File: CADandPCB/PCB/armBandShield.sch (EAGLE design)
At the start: 32 parts, among them Q1 BSS138, Q2 BSS138, U2 MPU-6050-1

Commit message: Initial layout 95% complete
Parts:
- removed FSR_HEADERS: (no value), SparkFun-Connectors:CONN_08"
- added J1: FSR_HEADERS_1, SparkFun-Connectors:CONN_04
- added J2: FSR_HEADERS_2, SparkFun-Connectors:CONN_04
- BT_HEADERS: value (none) -> J5
- LEFT_HEADER: value (none) -> J3
- RIGHT_HEADER: value (none) -> J4; device SparkFun-Connectors:CONN_15 -> SparkFun-Connectors:CONN_14
- SWITCH_HEADERS: value 455-1750-1-ND -> J8
- VCC_HEADERS: value (none) -> J6; device SparkFun-Connectors:CONN_02 -> SparkFun-Connectors:CONN_02PTH3
- VIN_HEADERS: value (none) -> J7
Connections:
- net A0: now also RIGHT_HEADER.3; no longer RIGHT_HEADER.4
- net A4/SDA/HIGH: now also RIGHT_HEADER.7; no longer RIGHT_HEADER.8
- net A5/SCL/HIGH: now also RIGHT_HEADER.8; no longer RIGHT_HEADER.9
- net FSR1: now also J2.1; no longer FSR_HEADERS.1
- net FSR2: now also J2.2; no longer FSR_HEADERS.2
- net FSR3: now also J2.3; no longer FSR_HEADERS.3
- net FSR4: now also J2.4; no longer FSR_HEADERS.4
- net FSR5: now also J1.1; no longer FSR_HEADERS.5
- net FSR6: now also J1.2; no longer FSR_HEADERS.6
- net FSR7: now also J1.3; no longer FSR_HEADERS.7
- net FSR8: now also J1.4; no longer FSR_HEADERS.8
- net GND: now also RIGHT_HEADER.13; no longer RIGHT_HEADER.14
- net VCC: now also RIGHT_HEADER.11; no longer RIGHT_HEADER.12
- net VCC_2: now also RIGHT_HEADER.1; no longer RIGHT_HEADER.2
- net VIN: now also RIGHT_HEADER.14; no longer RIGHT_HEADER.15

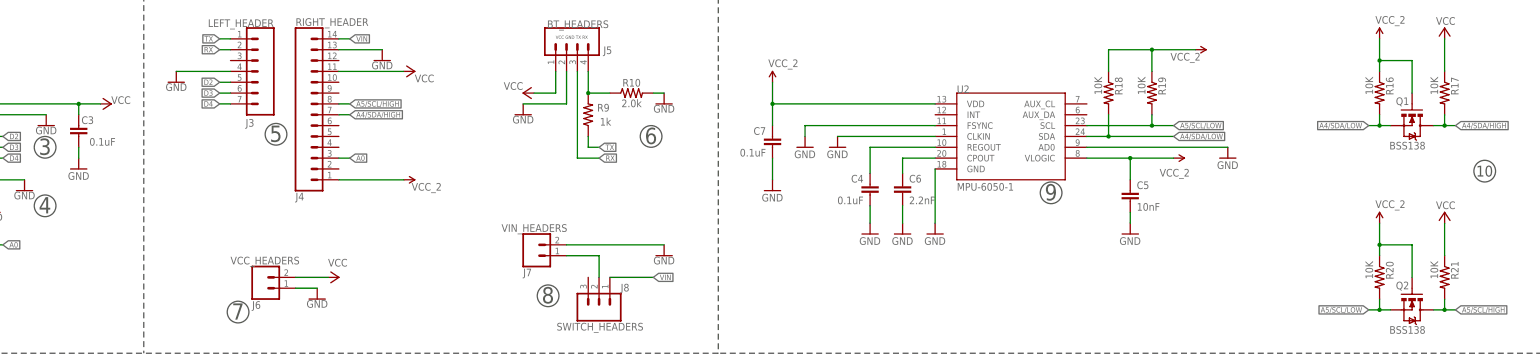
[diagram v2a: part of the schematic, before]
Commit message: Update trace sizes, pad extensions, silkscreen, and some routing.
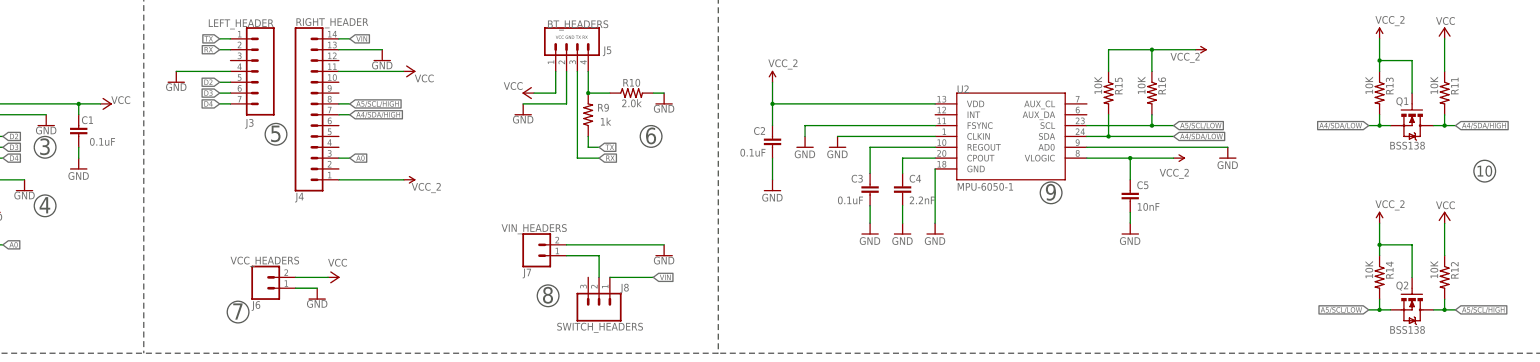
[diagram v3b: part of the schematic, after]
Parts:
- removed C6: 2.2nF, SparkFun-Capacitors:2.2NF/2200PF-0603-50V-10%
- removed R19: 10K, SparkFun-Resistors:10KOHM-1/10W-1%(0603)0603
- added C1: 0.1uF, SparkFun-Capacitors:0.1UF-25V(+80/-20%)(0603)
- added R13: 10K, SparkFun:RESISTOR0603-RES
- C4: value 0.1uF -> 2.2nF; device SparkFun-Capacitors:0.1UF-25V(+80/-20%)(0603) -> SparkFun-Capacitors:2.2NF/2200PF-0603-50V-10%
- R16: device SparkFun:RESISTOR0603-RES -> SparkFun-Resistors:10KOHM-1/10W-1%(0603)0603
- renumbered C7 to C2, R17 to R11, R18 to R15, R20 to R14, R21 to R12
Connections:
- net A4/SDA/LOW: now also R13.2; no longer R16.2
- net A5/SCL/LOW: now also R16.2; no longer R19.2
- net GND: now also C1.2; no longer C6.2
- net N$3: now also C4.1; no longer C6.1
- net N$5: now also C3.1; no longer C4.1
- net VCC: now also C1.1; no longer C3.1
- net VCC_2: now also R13.1; no longer R19.1
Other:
- moved on the sheet: C3, C4, R16

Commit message: Commit Gerber files and final rev 1 of board.
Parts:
- removed SWITCH_HEADERS: J8, SparkFun-Connectors:CONN_03
- added J10, J8, J9: (no value), SparkFun-Connectors:CONN_01
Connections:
- net N$1: now also J9.1; no longer SWITCH_HEADERS.2
- net VIN: now also J10.1; no longer SWITCH_HEADERS.1
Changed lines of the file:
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@@
 <?xml version="1.0" encoding="utf-8"?>
 <!DOCTYPE eagle SYSTEM "eagle.dtd">
-<eagle version="9.3.0">
+<eagle version="9.3.1">
 <drawing>
 <settings>
@@
 <part name="C5" library="SparkFun-Capacitors" deviceset="10NF" device="-0603-50V-10%" value="10nF"/>
 <part name="GND30" library="SparkFun-Aesthetics" deviceset="GND" device=""/>
-<part name="SWITCH_HEADERS" library="SparkFun-Connectors" deviceset="CONN_03" device="" value="J8"/>
 <part name="VCC_HEADERS" library="SparkFun-Connectors" deviceset="CONN_02" device="PTH3" value="J6"/>
 <part name="J1" library="SparkFun-Connectors" deviceset="CONN_04" device="" value="FSR_HEADERS_1"/>
 <part name="J2" library="SparkFun-Connectors" deviceset="CONN_04" device="" value="FSR_HEADERS_2"/>
 <part name="RIGHT_HEADER" library="SparkFun-Connectors" deviceset="CONN_14" device="" value="J4"/>
+<part name="J8" library="SparkFun-Connectors" deviceset="CONN_01" device=""/>
+<part name="J9" library="SparkFun-Connectors" deviceset="CONN_01" device=""/>
+<part name="J10" library="SparkFun-Connectors" deviceset="CONN_01" device=""/>
 </parts>
 <sheets>
@@
 <attribute name="VALUE" x="342.9" y="25.4" size="1.778" layer="96"/>
 </instance>
-<instance part="SWITCH_HEADERS" gate="J$1" x="220.98" y="10.16" smashed="yes" rot="R90">
-<attribute name="VALUE" x="228.092" y="16.256" size="1.778" layer="96" font="vector" rot="R180"/>
-<attribute name="NAME" x="231.394" y="7.112" size="1.778" layer="95" font="vector" rot="R180"/>
-</instance>
 <instance part="VCC_HEADERS" gate="G$1" x="142.24" y="15.24" smashed="yes">
 <attribute name="VALUE" x="139.7" y="10.414" size="1.778" layer="96" font="vector"/>
@@
 <attribute name="VALUE" x="149.86" y="35.814" size="1.778" layer="96" font="vector"/>
 <attribute name="NAME" x="149.86" y="76.708" size="1.778" layer="95" font="vector"/>
+</instance>
+<instance part="J8" gate="G$1" x="215.9" y="10.16" smashed="yes" rot="R90">
+<attribute name="VALUE" x="220.726" y="7.62" size="1.778" layer="96" font="vector" rot="R90"/>
+<attribute name="NAME" x="215.9" y="7.112" size="1.778" layer="95" font="vector" rot="R180" align="bottom-center"/>
+</instance>
+<instance part="J9" gate="G$1" x="220.98" y="10.16" smashed="yes" rot="R90">
+<attribute name="VALUE" x="225.806" y="7.62" size="1.778" layer="96" font="vector" rot="R90"/>
+<attribute name="NAME" x="220.98" y="7.112" size="1.778" layer="95" font="vector" rot="R180" align="bottom-center"/>
+</instance>
+<instance part="J10" gate="G$1" x="226.06" y="10.16" smashed="yes" rot="R90">
+<attribute name="VALUE" x="230.886" y="7.62" size="1.778" layer="96" font="vector" rot="R90"/>
+<attribute name="NAME" x="226.06" y="7.112" size="1.778" layer="95" font="vector" rot="R180" align="bottom-center"/>
 </instance>
 </instances>
@@
 </segment>
 <segment>
-<wire x1="223.52" y1="17.78" x2="233.68" y2="17.78" width="0.1524" layer="91"/>
 <label x="233.68" y="17.78" size="1.27" layer="95" xref="yes"/>
-<pinref part="SWITCH_HEADERS" gate="J$1" pin="1"/>
+<pinref part="J10" gate="G$1" pin="1"/>
+<wire x1="226.06" y1="17.78" x2="233.68" y2="17.78" width="0.1524" layer="91"/>
 </segment>
 </net>
@@
 <wire x1="213.36" y1="22.86" x2="220.98" y2="22.86" width="0.1524" layer="91"/>
 <wire x1="220.98" y1="22.86" x2="220.98" y2="17.78" width="0.1524" layer="91"/>
-<pinref part="SWITCH_HEADERS" gate="J$1" pin="2"/>
-</segment>
-</net>
+<pinref part="J9" gate="G$1" pin="1"/>
+</segment>
+</net>
